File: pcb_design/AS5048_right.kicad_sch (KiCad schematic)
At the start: 6 parts, among them J5 AS5600_Right, U7 AS5048B-HTSP

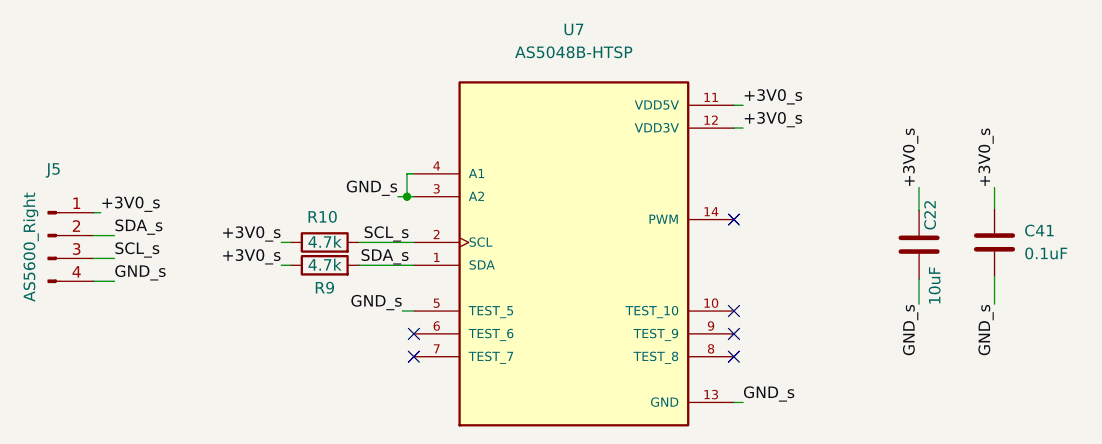
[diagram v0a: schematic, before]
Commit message: Update Mushak PCB design to include new features (#5)
* Update mushak PCB with new changes
* Add AMS1117 as 3.3v regulator
* Add new alternate placement for IR sensors
* Add new 3.3v compatible ToF sensor
* Update gerber files

* Add changes to silkscreen and filter capacitors
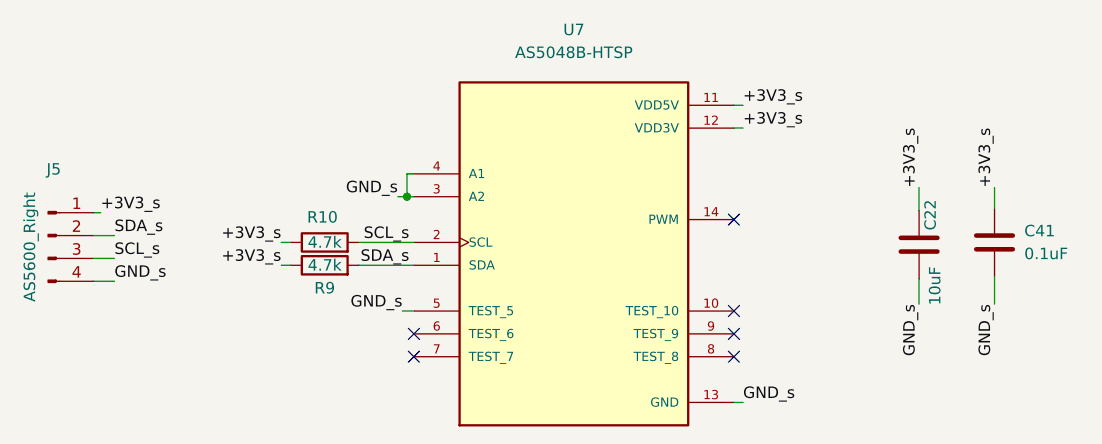
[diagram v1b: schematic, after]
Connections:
- net +3V0_s renamed +3V3_s
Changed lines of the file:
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@@
     (stroke (width 0) (type default) (color 0 0 0 0))
   )
-  (label "+3V0_s" (at 182.118 85.344 0)
+  (label "+3V3_s" (at 182.118 85.344 0)
     (effects (font (size 1.27 1.27)) (justify left bottom))
   )
-  (label "+3V0_s" (at 201.676 91.948 90)
+  (label "+3V3_s" (at 201.676 91.948 90)
     (effects (font (size 1.27 1.27)) (justify left bottom))
   )
@@
     (effects (font (size 1.27 1.27)) (justify right bottom))
   )
-  (label "+3V0_s" (at 182.118 82.804 0)
+  (label "+3V3_s" (at 182.118 82.804 0)
     (effects (font (size 1.27 1.27)) (justify left bottom))
   )
-  (label "+3V0_s" (at 130.81 98.044 180)
+  (label "+3V3_s" (at 130.81 98.044 180)
     (effects (font (size 1.27 1.27)) (justify right bottom))
   )
@@
     (effects (font (size 1.27 1.27)) (justify left bottom))
   )
-  (label "+3V0_s" (at 130.81 100.584 180)
+  (label "+3V3_s" (at 130.81 100.584 180)
     (effects (font (size 1.27 1.27)) (justify right bottom))
   )
@@
     (effects (font (size 1.27 1.27)) (justify right bottom))
   )
-  (label "+3V0_s" (at 210.058 91.948 90)
+  (label "+3V3_s" (at 210.058 91.948 90)
     (effects (font (size 1.27 1.27)) (justify left bottom))
   )
@@
     (effects (font (size 1.27 1.27)) (justify right bottom))
   )
-  (label "+3V0_s" (at 110.744 94.742 0)
+  (label "+3V3_s" (at 110.744 94.742 0)
     (effects (font (size 1.27 1.27)) (justify left bottom))
   )
